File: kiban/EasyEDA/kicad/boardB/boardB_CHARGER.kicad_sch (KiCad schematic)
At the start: 33 parts, among them U1 BQ25792

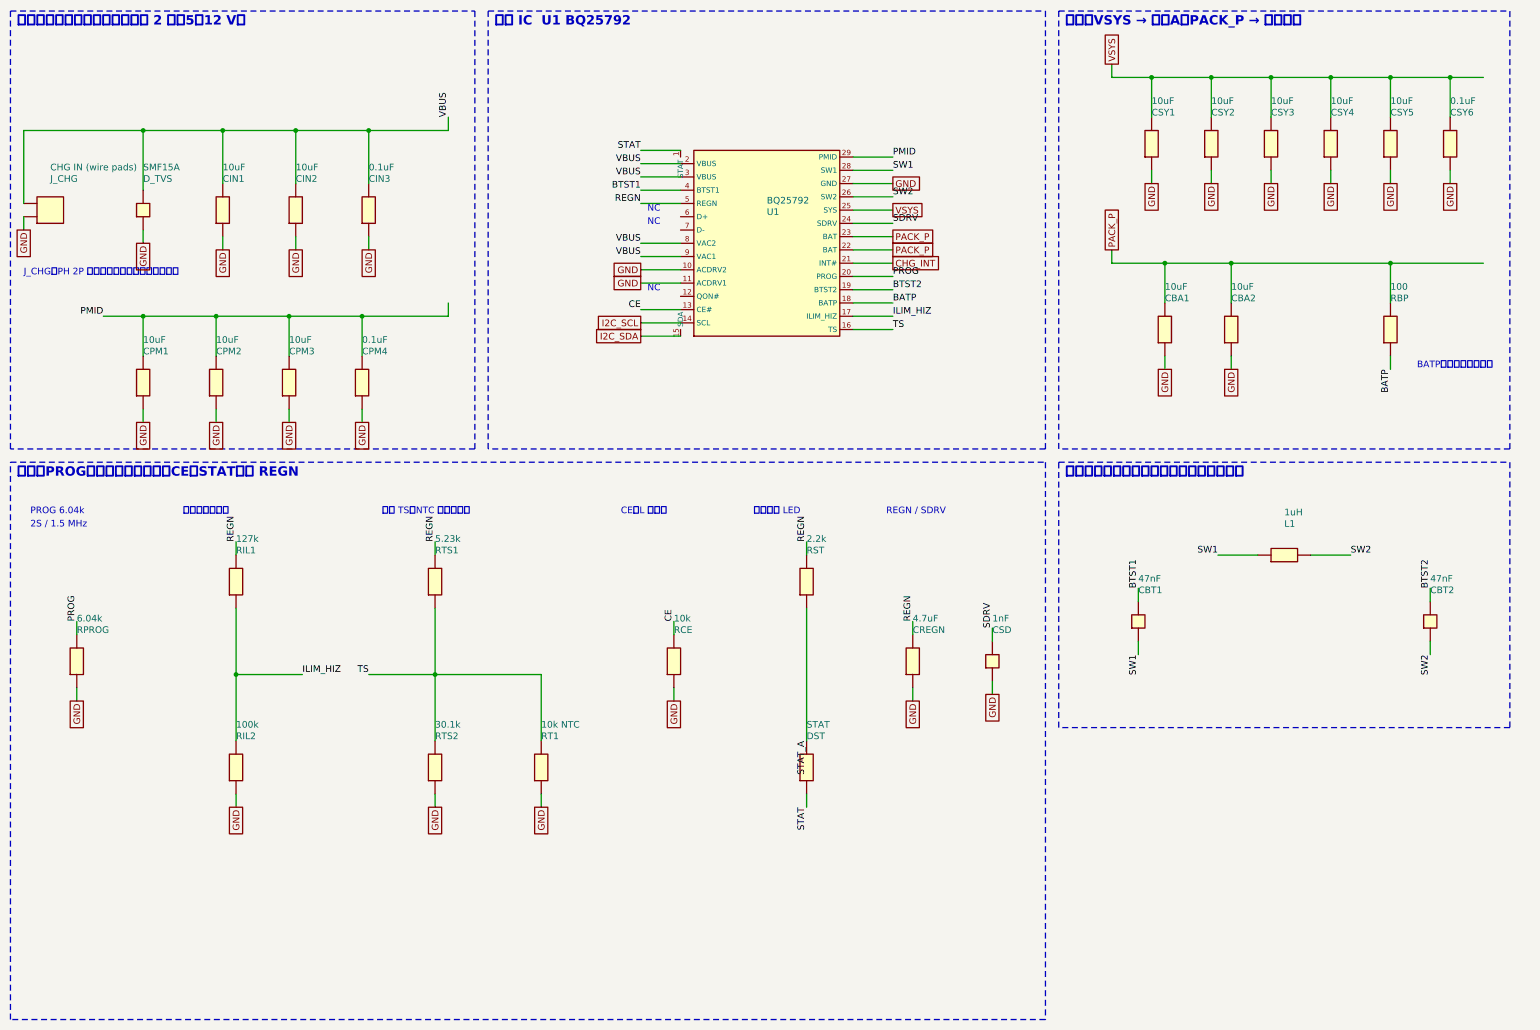
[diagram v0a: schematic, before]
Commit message: feat: KiCad 版の回路図に LCSC のシンボル・フットプリントを使う (easyeda2kicad)
- tools/kicad/lcsc_lib.py: LCSC 部品を easyeda2kicad で取得し、3D パスを直して KiCad 10 形式に更新、
  boardA / boardB に lcsc ライブラリを登録 (未取得の部品だけを、間隔を空けて取得)
- kicad_export.py: 取得したシンボルを、EasyEDA とピン位置が一致する向きで使い、フットプリントを割り当てる
  (合わない部品と未取得の部品は従来の矩形シンボル)。回転した部品の値の文字は横書きのまま
- 47 種類中 30 種類を取得 (残りは EasyEDA API の 403 で未取得)。111 部品中 82 部品が LCSC のシンボル
- kicad-cli のネットリストは基板A 23 / 基板B 43 ネットとも EasyEDA と一致
- 3D モデル (lcsc.3dshapes) と KiCad の .history/ は Git に入れない

Co-Authored-By: Claude Opus 5.5 <noreply@anthropic.com>
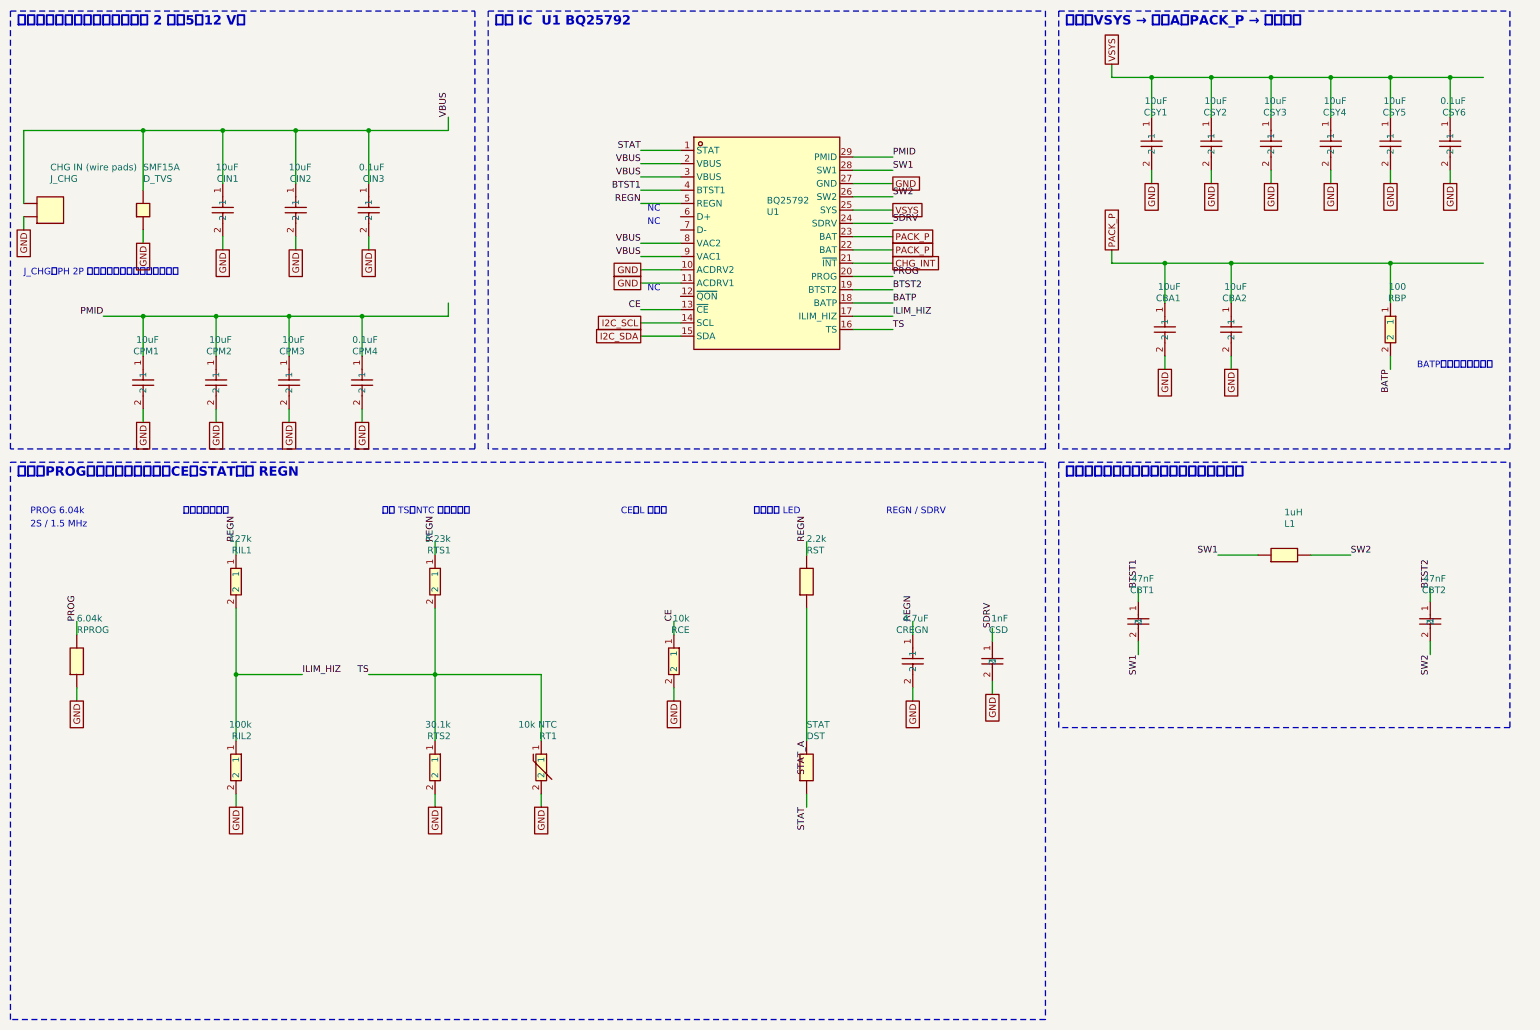
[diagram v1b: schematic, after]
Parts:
- CBA1, CBA2: footprint (none) -> lcsc:C0805; symbol gen:CBA_C15850_r270 -> lcsc:CL21A106KAYNNNE
- CBT1, CBT2: footprint (none) -> lcsc:C0603; symbol gen:CBT_C1622_r270 -> lcsc:CL10B473KB8NNNC
- CIN1, CIN2: footprint (none) -> lcsc:C0805; symbol gen:CIN_C15850_r270 -> lcsc:CL21A106KAYNNNE
- CIN3: footprint (none) -> lcsc:C0603; symbol gen:CIN_C1591_r270 -> lcsc:CL10B104KB8NNNC
- CPM1, CPM2, CPM3: footprint (none) -> lcsc:C0805; symbol gen:CPM_C15850_r270 -> lcsc:CL21A106KAYNNNE
- CPM4: footprint (none) -> lcsc:C0603; symbol gen:CPM_C1591_r270 -> lcsc:CL10B104KB8NNNC
- CREGN: footprint (none) -> lcsc:C0603; symbol gen:CREGN_C19666_r270 -> lcsc:CL10A475KO8NNNC
- CSD: footprint (none) -> lcsc:C0603; symbol gen:CSD_C1588_r270 -> lcsc:CL10B102KB8NNNC
- CSY1, CSY2, CSY3, CSY4, CSY5: footprint (none) -> lcsc:C0805; symbol gen:CSY_C15850_r270 -> lcsc:CL21A106KAYNNNE
- CSY6: footprint (none) -> lcsc:C0603; symbol gen:CSY_C1591_r270 -> lcsc:CL10B104KB8NNNC
- RBP: footprint (none) -> lcsc:R0603; symbol gen:RBP_C22775_r270 -> lcsc:0603WAF1000T5E
- RCE: footprint (none) -> lcsc:R0603; symbol gen:RCE_C25804_r270 -> lcsc:0603WAF1002T5E
- RIL1: footprint (none) -> lcsc:R0603; symbol gen:RIL_C22869_r270 -> lcsc:0603WAF1273T5E
- RIL2: footprint (none) -> lcsc:R0603; symbol gen:RIL_C25803_r270 -> lcsc:0603WAF1003T5E
- RT1: footprint (none) -> lcsc:R0603; symbol gen:RT_C13564_r270 -> lcsc:NCP18XH103F03RB
- RTS1: footprint (none) -> lcsc:R0603; symbol gen:RTS_C23068_r270 -> lcsc:0603WAF5231T5E
- RTS2: footprint (none) -> lcsc:R0603; symbol gen:RTS_C23000_r270 -> lcsc:0603WAF3012T5E
- U1: footprint (none) -> lcsc:QFN-29_L4.0-W4.0-P0.40-TL-BQ25792RQMR; symbol gen:U_C2862876_r0 -> lcsc:BQ25792RQMR
